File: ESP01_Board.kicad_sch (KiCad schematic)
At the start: 44 parts, among them J1 Conn_01x02, J10 Vin, J2 Conn_01x02, J3 IN, J4 IN, J5 DHT11/22, J6 Conn_01x02, J7 IN, J8 RELAY, J9 USB_C_Receptacle_PowerOnly_6P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

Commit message: Conclusa la prima versione
 - Inserite le serigrafie e controllato il circuito
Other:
- company: (none) -> Alan Masutti
- title: (none) -> ESP01 Board
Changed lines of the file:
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@@
 (kicad_sch (version 20230121) (generator eeschema)
   (paper "A4")
+  (title_block
+    (title "ESP01 Board")
+    (date "2024-06-12")
+    (rev "Rev 1.0")
+    (company "Alan Masutti")
+  )
   (junction (at 265.43 93.98) (diameter 0) (color 0 0 0 0)
   )
@@
     (stroke (width 0) (type default))
   )
-  (label "Rno" (at 165.1 168.91 180)
+  (label "Rno" (at 165.1 168.91 180) (fields_autoplaced)
     (effects (font (size 1.27 1.27)) (justify right bottom))
   )

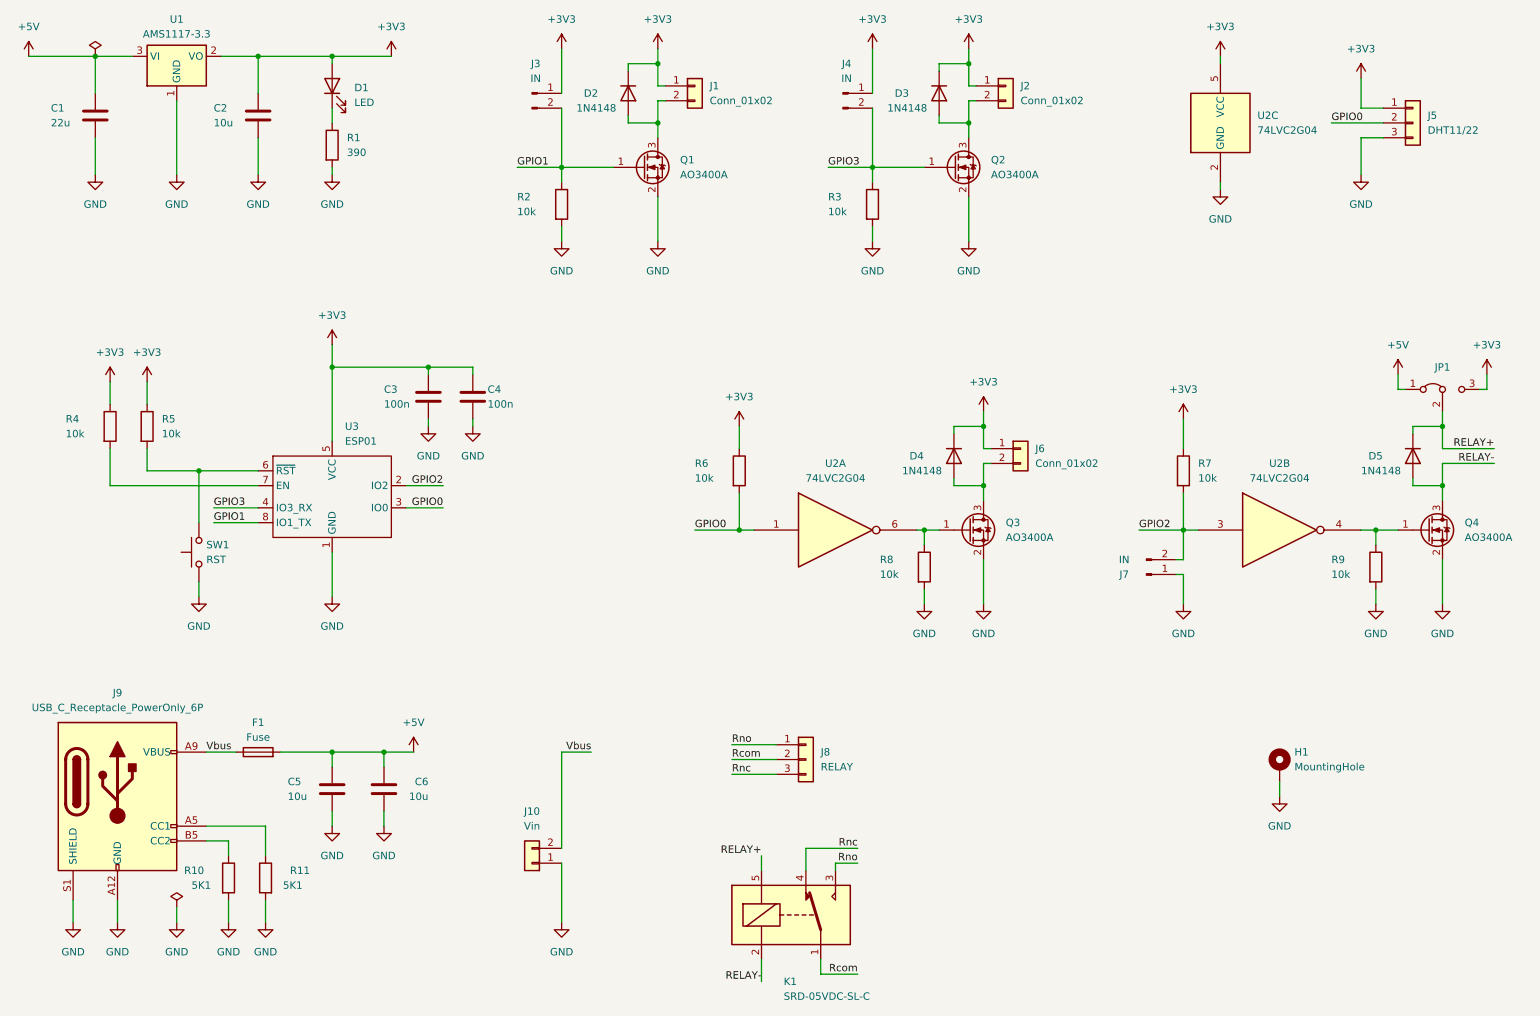
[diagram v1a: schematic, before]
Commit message: Modificato lo stadio di ingresso
 - Aggiunti i D-latch per l'utilizzo dei due GPIO di strapping

 - Corretto il Cartiglio dello schematico e compilato quello del foglio del PCB
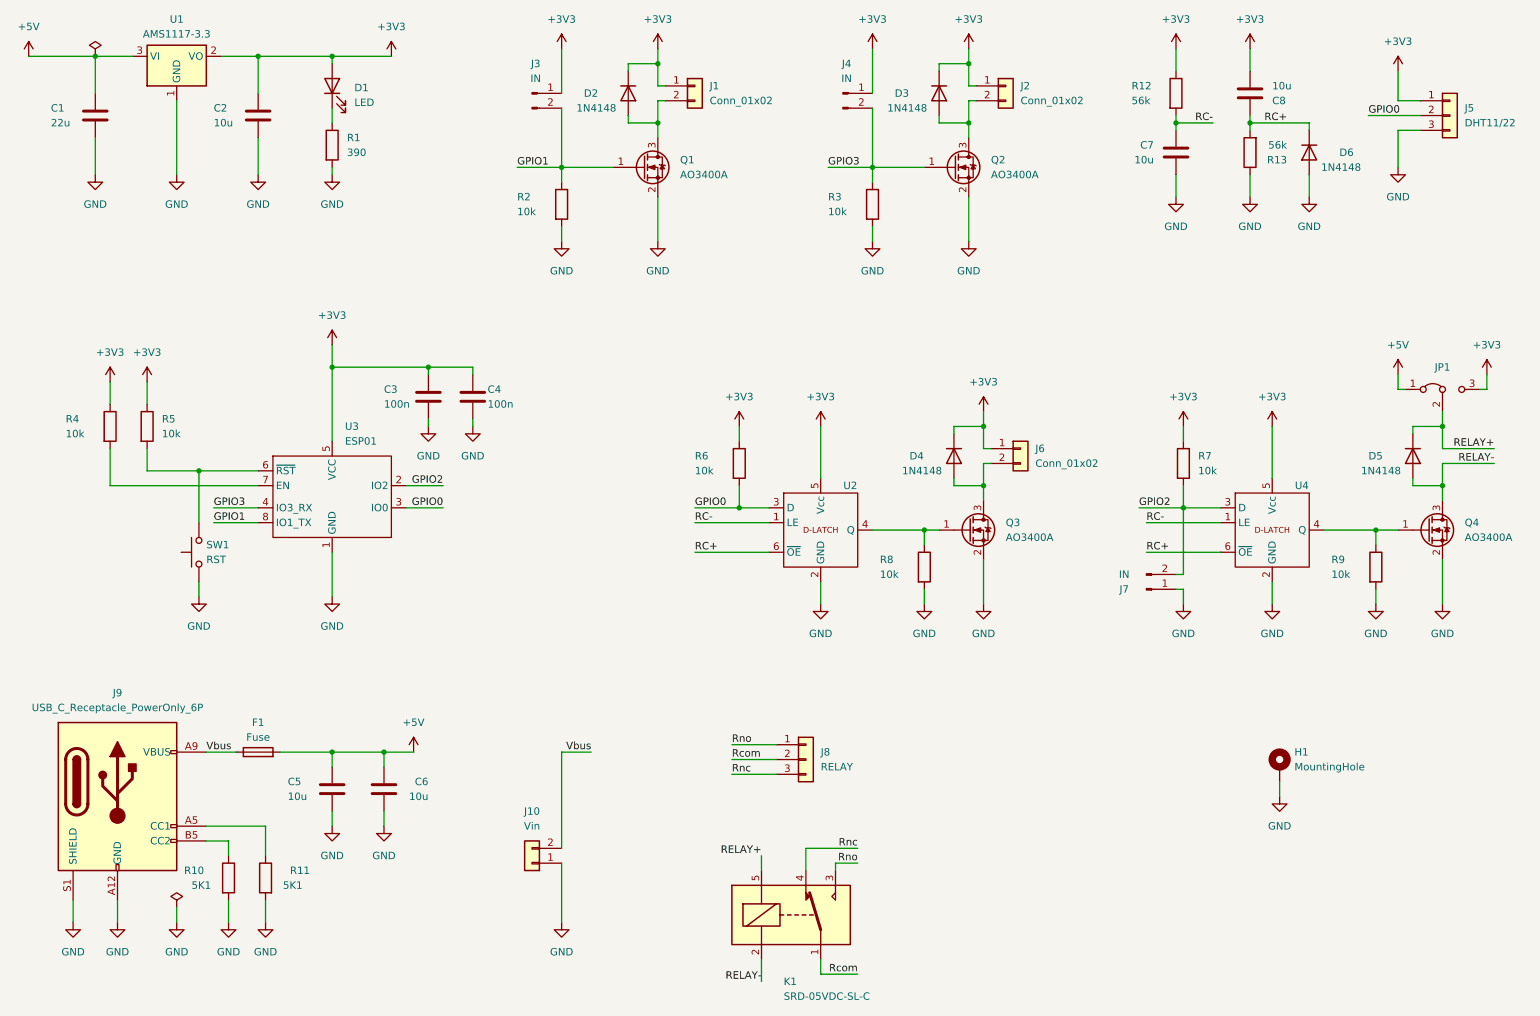
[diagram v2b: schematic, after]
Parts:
- removed U2: 74LVC2G04, Package_TO_SOT_SMD:SOT-23-6_Handsoldering, symbol 74xGxx:74LVC2G04
- added C7, C8: 10u, Capacitor_SMD:C_0805_2012Metric, symbol Device:C
- added D6: 1N4148, Diode_SMD:D_SOD-123, symbol Diode:1N4148
- added R12, R13: 56k, Resistor_SMD:R_0805_2012Metric, symbol Device:R
- added U2, U4: ~, Package_TO_SOT_SMD:SOT-363_SC-70-6_Handsoldering, symbol PersonalLibrary:74AUP1G373
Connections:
- net +3V3: now also C8.2, R12.1, U2.5 (Vcc), U4.5 (Vcc)
- net GND: now also C7.2, D6.2 (A), R13.1, U2.2 (GND), U4.2 (GND)
- net GPIO0: now also U2.3 (D)
- net GPIO2: now also U4.3 (D)
- net at Q3.1 (G), R8.1: now also U2.4 (Q)
- net at Q4.1 (G), R9.1: now also U4.4 (Q)
- new net RC+: C8.1, D6.1 (K), R13.2, U2.6 (~{OE}), U4.6 (~{OE})
- new net RC-: C7.1, R12.2, U2.1 (LE), U4.1 (LE)
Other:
- moved on the sheet: J5, J7, R6, R7

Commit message: Completata Rev1.1
 - Sistemati Errori di sovrascritture (Vedi ad esempio i cartigli)
 - Sistemata la BOM
 - Corrette le Serigrafie
 - Controllato il design
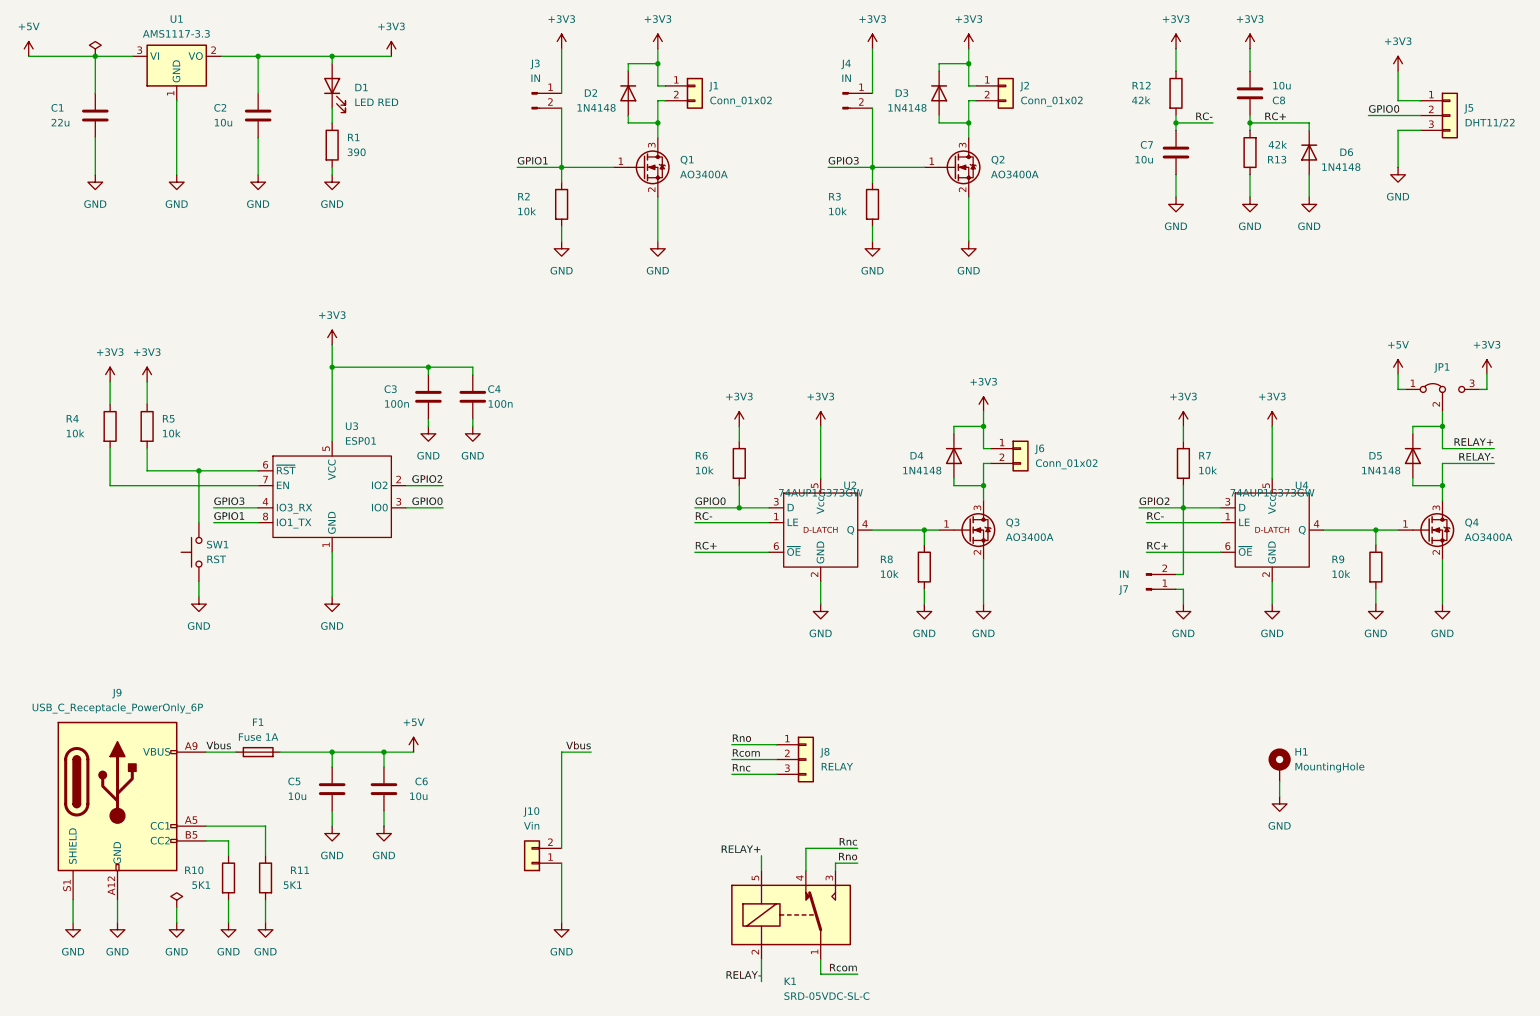
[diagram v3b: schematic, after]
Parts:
- D1: value LED -> LED RED
- F1: value Fuse -> Fuse 1A
- R12, R13: value 56k -> 42k
- U2, U4: value ~ -> 74AUP1G373GW; footprint Package_TO_SOT_SMD:SOT-363_SC-70-6_Handsoldering -> Package_TO_SOT_SMD:SOT-363_SC-70-6
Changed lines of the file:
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@@
   (title_block
     (title "ESP01 Board")
-    (date "2024-06-12")
-    (rev "Rev 1.0")
+    (date "2024-06-15")
+    (rev "Rev 1.1")
     (company "Alan Masutti")
   )
@@
       (effects (font (size 1.27 1.27)) (justify left))
     )
-    (property "Value" "56k" (at 238.76 45.72 0)
+    (property "Value" "42k" (at 238.76 45.72 0)
       (effects (font (size 1.27 1.27)) (justify left))
     )
@@
       (effects (font (size 1.27 1.27)) hide)
     )
-    (property "Datasheet" "~" (at 156.21 151.13 0)
+    (property "Datasheet" "https://www.lcsc.com/datasheet/lcsc_datasheet_2304140030_Ningbo-Songle-Relay-SRD-05VDC-SL-C_C35449.pdf" (at 156.21 151.13 0)
       (effects (font (size 1.27 1.27)) hide)
     )
@@
       (effects (font (size 1.27 1.27)))
     )
-    (property "Value" "Fuse" (at 62.23 147.32 90)
+    (property "Value" "Fuse 1A" (at 62.23 147.32 90)
       (effects (font (size 1.27 1.27)))
     )
@@
       (effects (font (size 1.27 1.27)) (justify left))
     )
-    (property "Value" "56k" (at 212.09 38.1 0)
+    (property "Value" "42k" (at 212.09 38.1 0)
       (effects (font (size 1.27 1.27)) (justify left))
     )
@@
       (effects (font (size 1.27 1.27)) (justify right))
     )
-    (property "Value" "LED" (at 78.74 38.4175 90)
+    (property "Value" "LED RED" (at 78.74 38.4175 90)
       (effects (font (size 1.27 1.27)) (justify right))
     )
@@
       (effects (font (size 1.27 1.27)) (justify left) hide)
     )
-    (property "Datasheet" "http://www.sanyourelay.ca/public/products/pdf/SRD.pdf" (at 153.67 177.8 0)
+    (property "Datasheet" "https://www.lcsc.com/datasheet/lcsc_datasheet_2304140030_Ningbo-Songle-Relay-SRD-05VDC-SL-C_C35449.pdf" (at 153.67 177.8 0)
       (effects (font (size 1.27 1.27)) hide)
     )
@@
       (effects (font (size 1.27 1.27)) hide)
     )
-    (property "Datasheet" "" (at 74.93 99.06 0)
+    (property "Datasheet" "~" (at 74.93 99.06 0)
       (effects (font (size 1.27 1.27)) hide)
     )
@@
       (effects (font (size 1.27 1.27)))
     )
-    (property "Value" "~" (at 236.22 105.41 0)
-      (effects (font (size 1.27 1.27)))
-    )
-    (property "Footprint" "Package_TO_SOT_SMD:SOT-363_SC-70-6_Handsoldering" (at 236.22 105.41 0)
-      (effects (font (size 1.27 1.27)) hide)
-    )
-    (property "Datasheet" "" (at 236.22 105.41 0)
+    (property "Value" "74AUP1G373GW" (at 236.22 105.41 0)
+      (effects (font (size 1.27 1.27)))
+    )
+    (property "Footprint" "Package_TO_SOT_SMD:SOT-363_SC-70-6" (at 236.22 105.41 0)
+      (effects (font (size 1.27 1.27)) hide)
+    )
+    (property "Datasheet" "https://www.lcsc.com/datasheet/lcsc_datasheet_2005261506_Nexperia-74AUP1G373GW-125_C458800.pdf" (at 236.22 105.41 0)
       (effects (font (size 1.27 1.27)) hide)
     )
@@
     )
   )
-  (symbol (lib_id "PersonalLibrary:74AUP1G373") (at 158.75 105.41 0) (unit 1)
+  (symbol (lib_name "74AUP1G373_1") (lib_id "PersonalLibrary:74AUP1G373") (at 158.75 105.41 0) (unit 1)
     (in_bom yes) (on_board yes) (dnp no)
     (property "Reference" "U2" (at 163.83 104.14 0)
       (effects (font (size 1.27 1.27)))
     )
-    (property "Value" "~" (at 158.75 105.41 0)
-      (effects (font (size 1.27 1.27)))
-    )
-    (property "Footprint" "Package_TO_SOT_SMD:SOT-363_SC-70-6_Handsoldering" (at 158.75 105.41 0)
-      (effects (font (size 1.27 1.27)) hide)
-    )
-    (property "Datasheet" "" (at 158.75 105.41 0)
-      (effects (font (size 1.27 1.27)) hide)
-    )
+    (property "Value" "74AUP1G373GW" (at 158.75 105.41 0)
+      (effects (font (size 1.27 1.27)))
+    )
+    (property "Footprint" "Package_TO_SOT_SMD:SOT-363_SC-70-6" (at 158.75 105.41 0)
+      (effects (font (size 1.27 1.27)) hide)
+    )
+    (property "Datasheet" "https://www.lcsc.com/datasheet/lcsc_datasheet_2005261506_Nexperia-74AUP1G373GW-125_C458800.pdf" (at 158.75 105.41 0)
+      (effects (font (size 1.27 1.27)) hide)
+    )

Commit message: Aggiunti i codici LCSC + Aggiornato footprint del fuse
 - Aggiunta anche la serigrafia con il valore del fusibile,
 - Aggiornata la data sul foglio del PCB,
 - Ricreati i teardrop
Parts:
- C1: LCSC (none) -> C2918507
- C2, C5, C6, C7, C8: LCSC (none) -> C3015161
- C3, C4: LCSC (none) -> C2991409
- D1: LCSC (none) -> C7496834
- D2, D3, D4, D5, D6: LCSC (none) -> C7420318
- F1: footprint Fuse:Fuse_0805_2012Metric_Pad1.15x1.40mm_HandSolder -> Fuse:Fuse_1206_3216Metric_Pad1.42x1.75mm_HandSolder; LCSC (none) -> C151135
- J8, K1: LCSC (none) -> C35449
- J9: LCSC (none) -> C2927027
- Q1, Q2, Q3, Q4: LCSC (none) -> C347475
- R1: LCSC (none) -> C17655
- R10, R11: LCSC (none) -> C27834
- R12, R13: LCSC (none) -> C4151965
- R2, R3, R4, R5, R6, R7, R8, R9: LCSC (none) -> C17414
- U1: LCSC (none) -> C5120765
- U2, U4: LCSC (none) -> C458800
